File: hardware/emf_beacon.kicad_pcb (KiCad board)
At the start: 2 copper layers, 100 x 100 mm, 134 parts, among them J1 USB_C_Receptacle_USB2.0_16P, J10 Conn_01x02, J11 Conn_01x02, J12 Conn_01x02, J13 Conn_01x02, J14 Conn_01x02, J2 B6B-PH-SM4-TB, J3 B6B-PH-SM4-TB, J4 Conn_01x02, J5 Conn_01x02, J6 Conn_01x02, J7 Conn_01x02, J8 Conn_01x02, J9 Conn_01x02, Q1 AO3400A, Q10 AO3400A, Q12 DMP3013SFV, Q2 AO3400A, Q3 AO3400A, Q4 AO3400A, Q5 AO3400A, Q6 AO3400A, Q7 AO3400A, Q8 AO3400A, Q9 AO3400A, SW1 SW_DIP_x10, SW2 TS-1088-AR02016, U1 ESP32-C3-WROOM-02, U2 MCP23017T-E/SS, U4 PCA9685PW,118, U5 TPS565208, U6 CA-IS3092VW, U7 TPS82140SILR

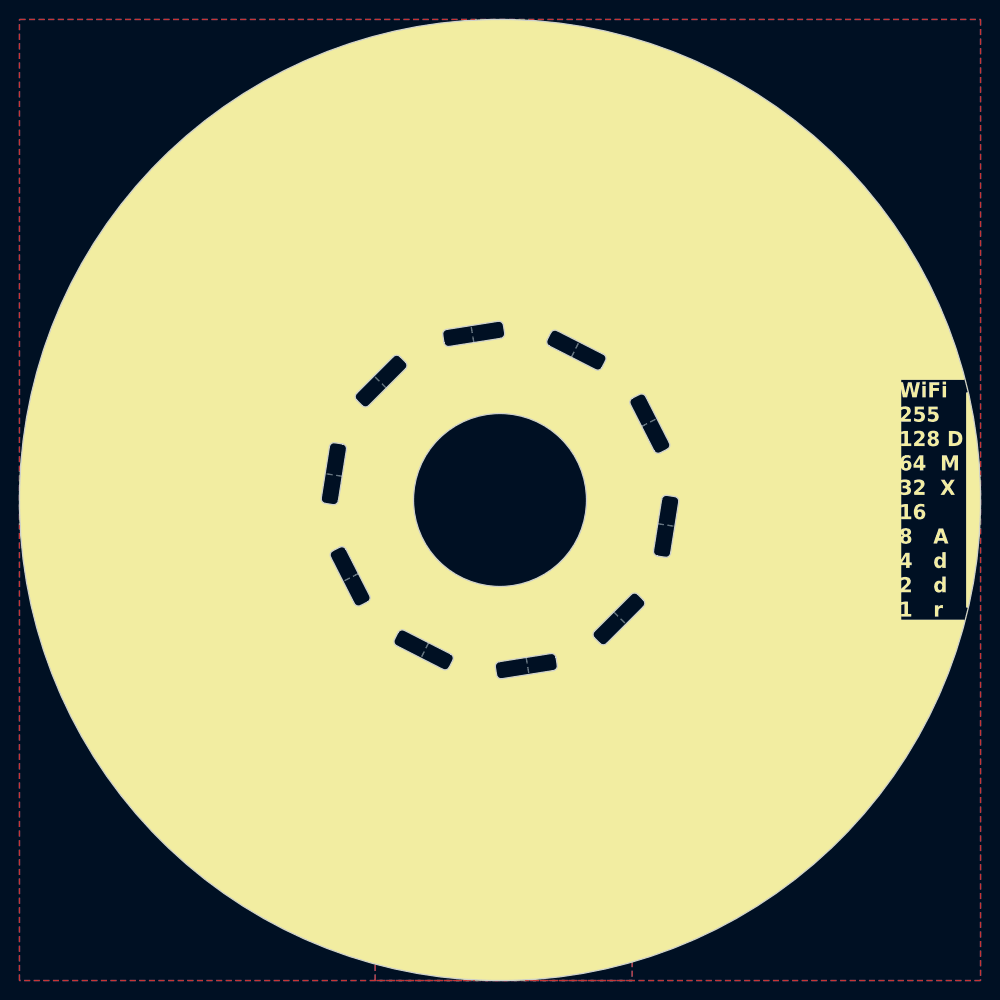
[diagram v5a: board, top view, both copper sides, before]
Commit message: LEDs connected
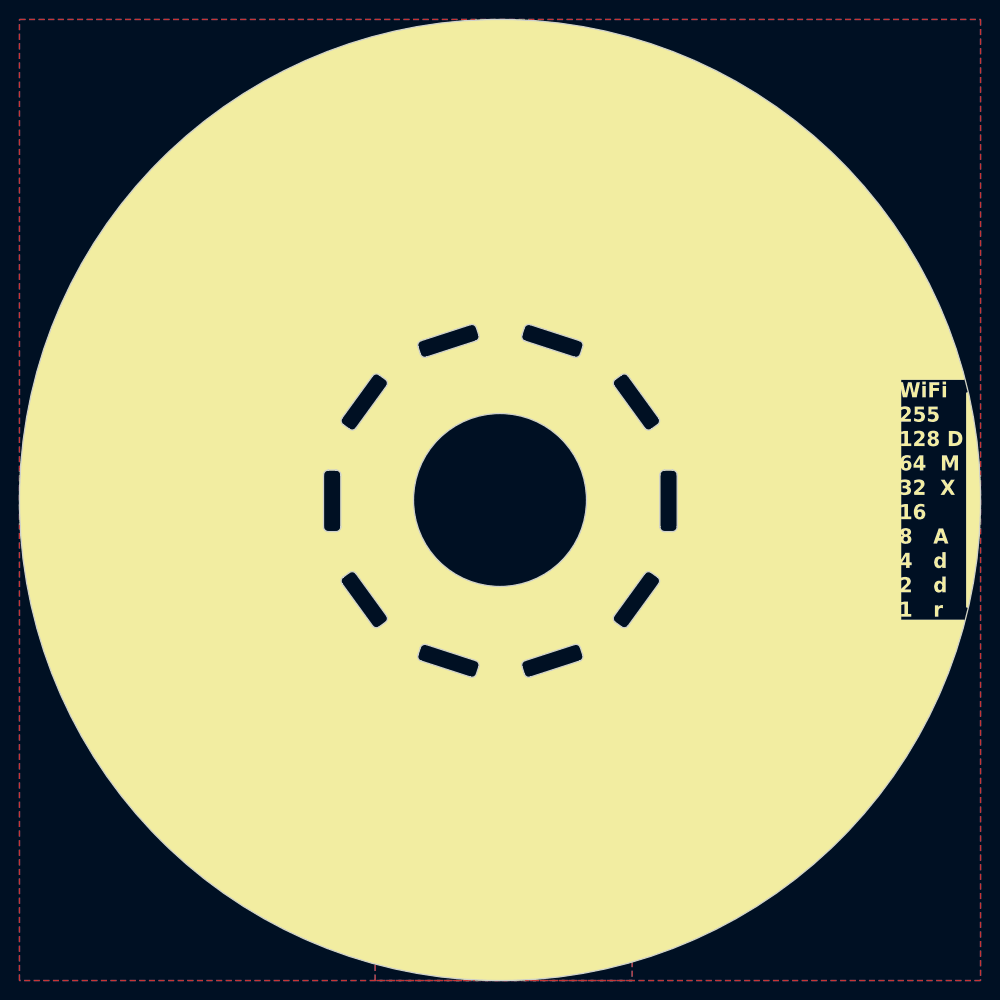
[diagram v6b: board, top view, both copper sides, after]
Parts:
- moved C16 48.0 mm to (124.5, 107.1)
- moved TP7 21.8 mm to (163.5, 100.0)
- moved C30 18.8 mm to (153.4, 124.1), turned to 108 degrees
- moved C32 18.7 mm to (128.1, 110.7), turned to 36 degrees
- moved C36 18.7 mm to (161.5, 78.5), turned to -108 degrees
- moved C31 18.6 mm to (138.5, 121.5), turned to 72 degrees
- moved C35 18.6 mm to (146.6, 75.9), turned to -72 degrees
- moved C29 18.6 mm to (166.9, 117.5), turned to 144 degrees
- moved R18 18.5 mm to (158.5, 122.0), turned to 108 degrees
- moved C37 18.5 mm to (171.9, 89.3), turned to -144 degrees
- moved R17 18.4 mm to (169.7, 112.8), turned to 144 degrees
- moved C28 18.4 mm to (174.0, 104.2), turned to 180 degrees
- moved C33 18.4 mm to (126.0, 95.8), turned to 0 degrees
- moved C34 18.3 mm to (133.1, 82.5), turned to -36 degrees
- moved R24 18.3 mm to (156.1, 77.3), turned to -108 degrees
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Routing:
- net +6V5: track 40.8 -> 143.6 mm
- net /LEDS/LED5: track 0.00 -> 68.9 mm, vias 0 -> 2
- net /LEDS/LED6: track 0.00 -> 58.9 mm, vias 0 -> 2
- net /LEDS/LED4: track 0.00 -> 58.8 mm, vias 0 -> 2
- net /LEDS/LED3: track 0.00 -> 50.8 mm, vias 0 -> 2
- net /LEDS/LED7: track 0.00 -> 48.7 mm, vias 0 -> 2
- net /LEDS/LED2: track 0.00 -> 40.6 mm
- net /LEDS/LED8: track 2.09 -> 38.1 mm, vias 0 -> 2
- net /I2C_~{INT}: track 35.1 -> 66.9 mm, vias 1 -> 2
- net /CTRL/DMX_RX: track 96.8 -> 119.1 mm
- net /CTRL/DMX_TX: track 96.9 -> 119.1 mm
- net /LEDS/LED1: track 0.00 -> 21.7 mm
- net /I2C_SDA: track 52.5 -> 73.4 mm, vias 2 -> 4
- net /I2C_SCL: track 50.6 -> 69.6 mm, vias 2 -> 4
- net /LEDS/LED9: track 2.05 -> 16.6 mm
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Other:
- board text added: "0V"
- board text added: "3V3"
- board text added: "6V5"
- board text added: "VDC"
- board text added: "VIN"

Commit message: updating DMX TRX and improving silkscreen
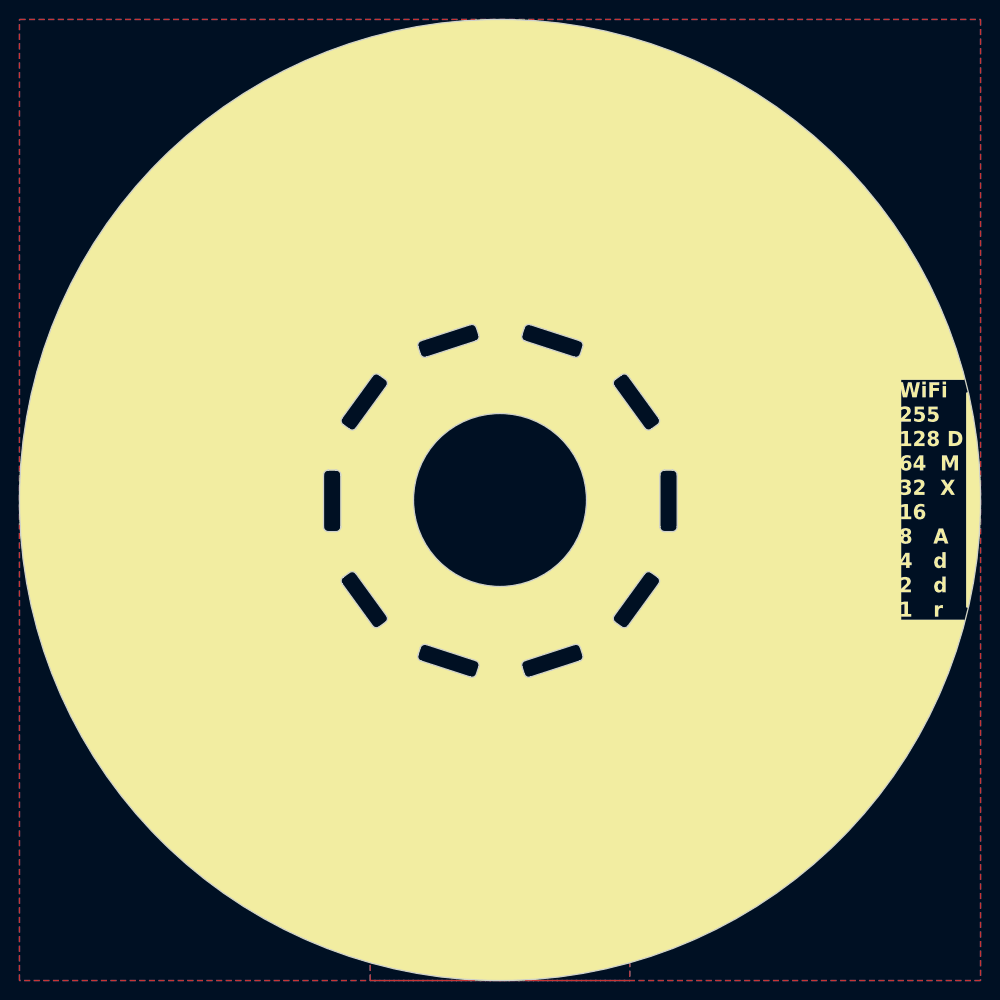
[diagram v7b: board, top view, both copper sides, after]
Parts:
- removed C23: 100nF, Capacitor_SMD:C_0603_1608Metric
- J10, J11, J12, J13, J4, J5, J6, J7, J8, J9: footprint emf_beacon_library:LED_Stick -> Pinski1_parts:LED_Stick
- U6: value CA-IS3092VW -> CA-IS3092W
- moved C3 48.9 mm to (134.2, 56.2)
- moved R3 45.4 mm to (132.8, 56.2), turned to 90 degrees
- moved TP6 15.7 mm to (109.5, 85.0)
- moved C14 4.60 mm to (131.8, 125.5), turned to 0 degrees
- moved TP1 3.05 mm to (123.0, 125.5), turned to 180 degrees
- moved R10 2.46 mm to (155.0, 139.0), turned to 90 degrees
- moved R11 2.46 mm to (155.0, 136.0), turned to 90 degrees
- moved R26 2.26 mm to (131.8, 123.8), turned to 0 degrees
- moved J14 1.33 mm to (128.5, 136.5)
- moved C7 1.27 mm to (157.2, 134.0)
- moved C5 0.88 mm to (155.6, 146.2)
- moved J2 0.88 mm to (141.4, 139.5)
- moved J3 0.88 mm to (150.4, 139.5)
- moved R8 0.88 mm to (158.1, 146.2)
- moved C8 0.78 mm to (159.0, 133.8)
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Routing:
- net +3V3_ISO: track 0.00 -> 21.9 mm, vias 0 -> 3
- net +3V3: track 228.5 -> 236.9 mm
- net /CTRL/TEMP_MON: track 0.00 -> 3.75 mm
- net /DMX512/DMX_DATA+: track 19.6 -> 20.1 mm
- net GND_ISO: vias 15 -> 19
- net GND: vias 75 -> 82
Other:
- board text added: "LED Beacon Null Sector 2026 v0"

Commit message: routing VDC
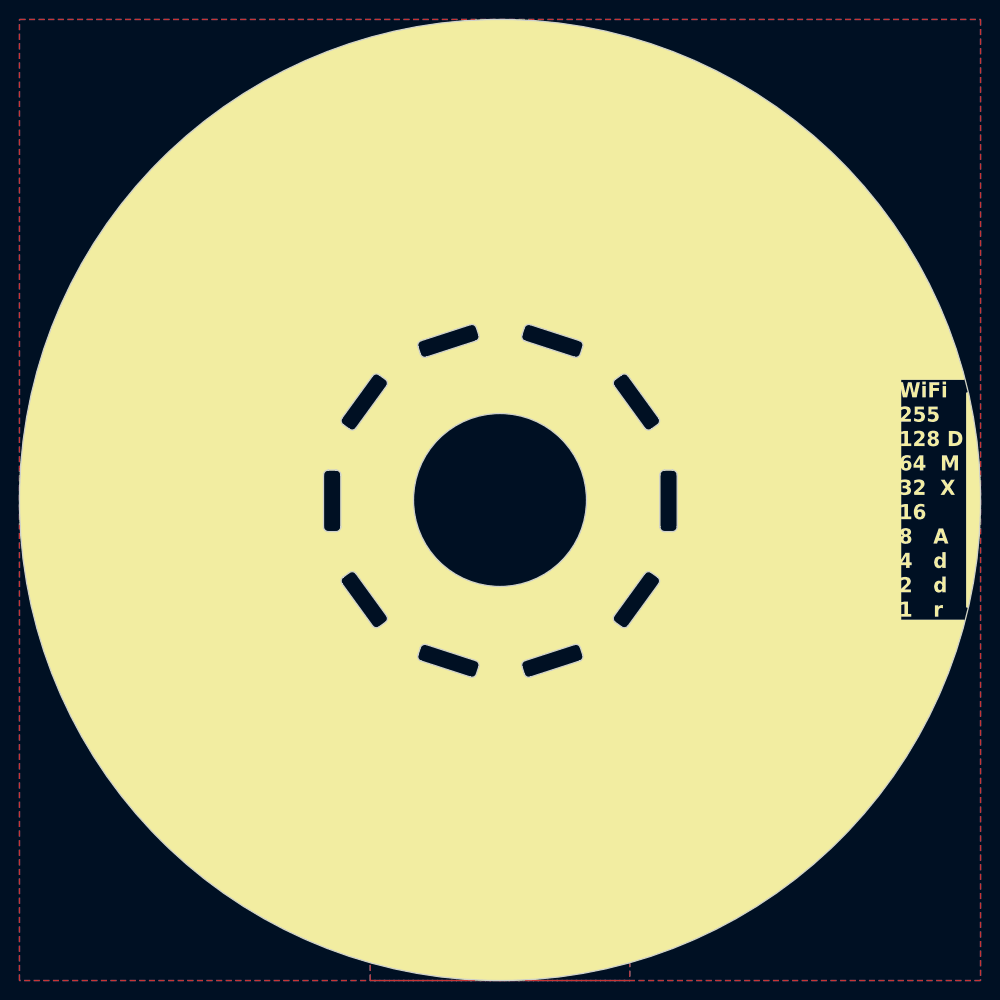
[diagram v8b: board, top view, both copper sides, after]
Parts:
- moved TP6 16.7 mm to (105.5, 101.2)
- moved D3 7.84 mm to (120.2, 118.3), turned to 45 degrees
- moved C15 7.40 mm to (112.2, 114.5), turned to 90 degrees
- moved R26 6.85 mm to (125.6, 120.6), turned to 45 degrees
- moved TP3 6.39 mm to (105.5, 107.8)
- moved C16 6.27 mm to (120.5, 102.2), turned to 90 degrees
- moved C14 6.07 mm to (126.9, 121.9), turned to 45 degrees
- moved D2 5.91 mm to (122.1, 120.9), turned to 45 degrees
- moved TP1 5.46 mm to (128.2, 124.0)
- moved Q12 4.09 mm to (124.0, 124.1), turned to -45 degrees
- moved TH1 3.91 mm to (117.5, 93.5)
- moved C12 3.89 mm to (114.2, 88.5)
- moved C13 3.89 mm to (109.2, 92.2)
- moved C17 3.89 mm to (107.2, 92.2)
- moved C18 3.89 mm to (113.8, 107.0)
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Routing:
- net /CTRL/TEMP_MON: track 3.75 -> 31.4 mm, vias 0 -> 1
- net +6V5: track 143.6 -> 163.7 mm
- net Net-(J14-Pin_2): track 0.00 -> 17.4 mm
- net VDC: track 100.6 -> 106.4 mm
- net Net-(D2-A): track 0.00 -> 4.56 mm
- net GND_ISO: vias 19 -> 30
- net GND: vias 82 -> 117
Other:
- board text added: "+ -"
- board text added: "+12V ~2A"
